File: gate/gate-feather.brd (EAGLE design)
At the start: 64.8 x 91.4 mm, 32 parts, among them J1 1X21X02-BIG, U1 SN75468

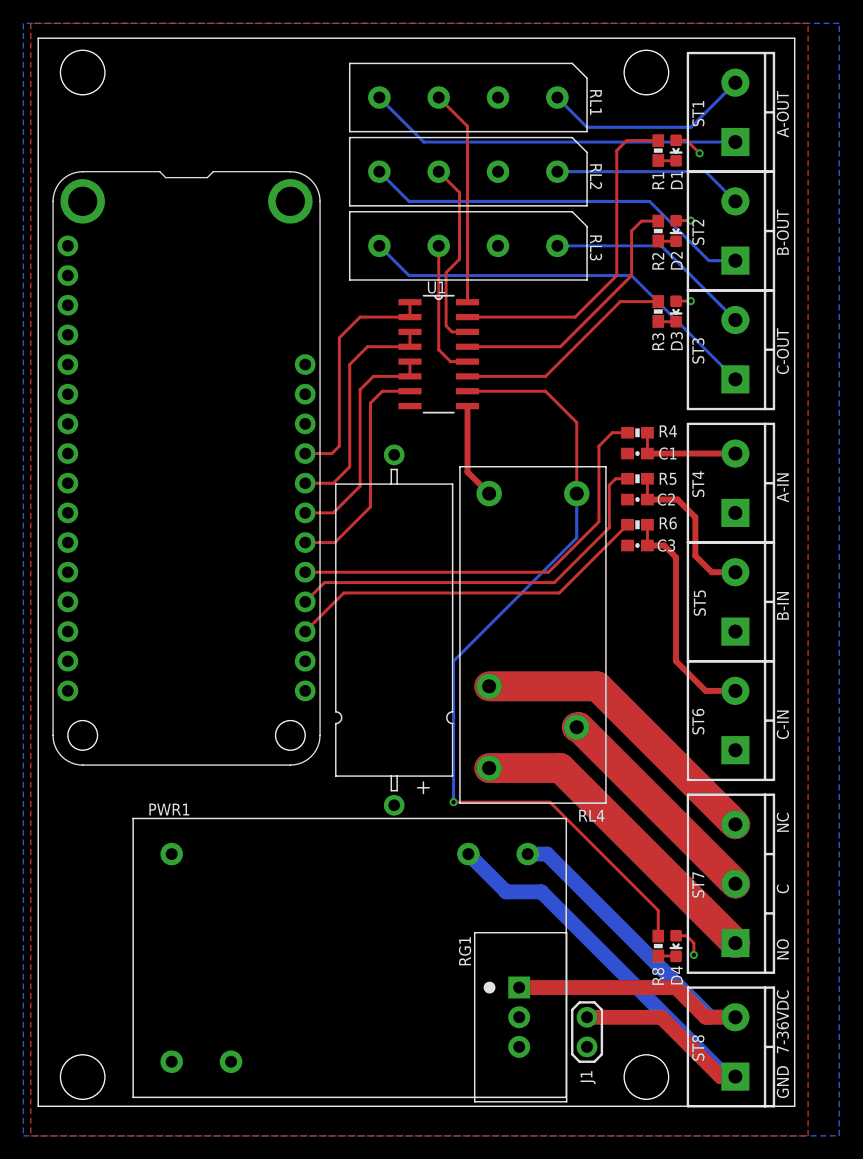
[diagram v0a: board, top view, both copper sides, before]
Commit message: New argon and feather boards
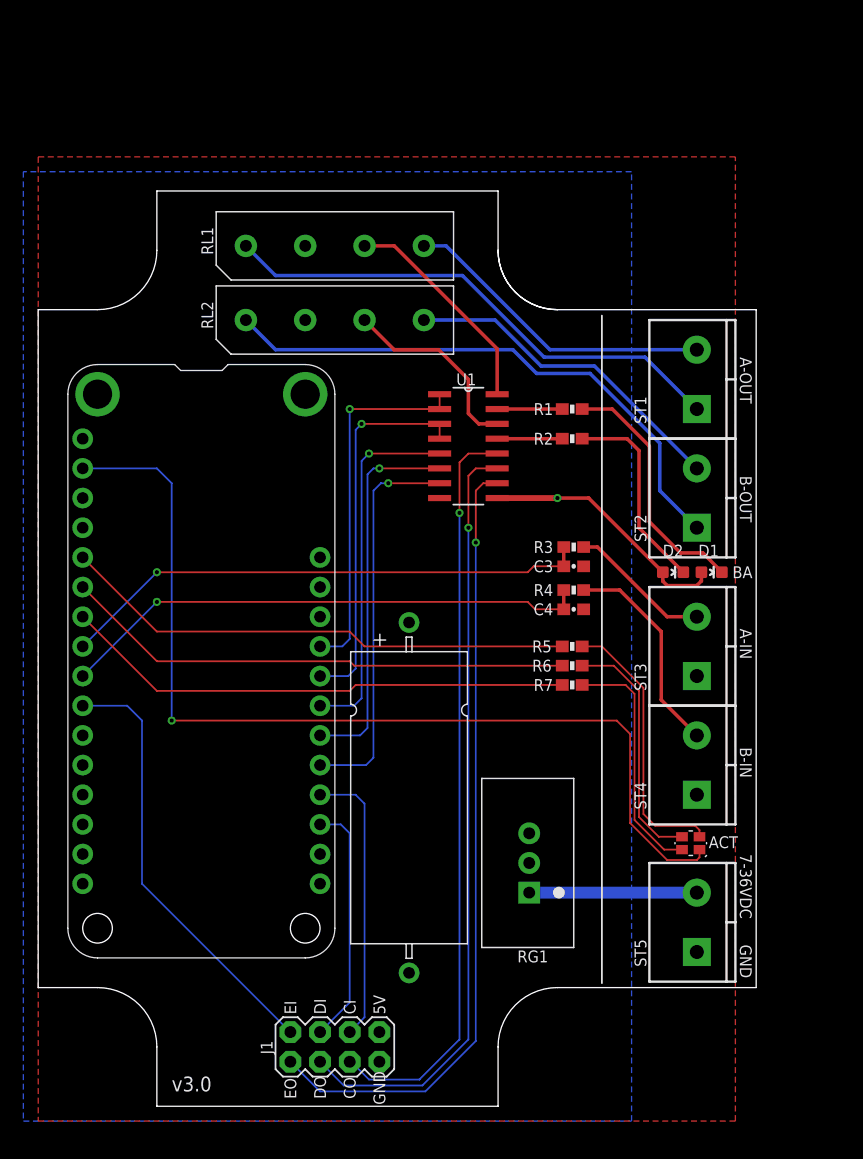
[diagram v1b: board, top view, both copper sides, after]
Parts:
- removed C2: .01u, SparkFun-Capacitors:0603-CAP
- removed D3, D4: (no value), SparkFun-LED:LED-0603
- removed MS2: FEATHERWING_NODIM, adafruit:FEATHERWING_DIM
- removed PWR1: IRM_03_PS_3W, Puffin:IRM_03_PS_3W
- removed R8: 2.2K, SparkFun-Resistors:0603-RES
- removed RL3: HE3600_RELAY, Puffin:HE3600_RELAY
- removed RL4: G2RL_SPDT, Puffin:G2RL_SPDT
- removed ST6, ST8: (no value), Puffin:SCREWTERM_0.2X2
- removed ST7: (no value), Puffin:SCREWTERM_0.2X3
- added LED1: LED-RGB-CREE-SMD, SomUSB1:LED-RGB-CREE-SMD
- added MS1: FEATHERWING_NODIM, adafruit:FEATHERWING_DIM
- added R7: 1K, SparkFun-Resistors:0603-RES
- C1: value .01u -> (none); device SparkFun-Capacitors:0603-CAP -> Puffin:CAP-AXIAL-10X25
- C4: value (none) -> .01u; device Puffin:CAP-AXIAL-10X25 -> SparkFun-Capacitors:0603-CAP
- J1: value 1X21X02-BIG -> (none); device Puffin:1X02-BIG -> SparkFun-Connectors:2X4
- R3: value 2.2K -> 1K
- moved D1 36.2 mm to (57.7, 45.7), turned to 270 degrees
- moved C1 35.4 mm to (31.8, 26.4), turned to 90 degrees
- moved RL1 29.5 mm to (17.8, 73.7), turned to 90 degrees
- moved RL2 29.5 mm to (17.8, 67.3), turned to 90 degrees
- moved D2 29.2 mm to (54.4, 45.7), turned to 270 degrees
- moved ST5 27.6 mm to (56.4, 13.2)
- moved ST3 25.6 mm to (56.4, 36.8)
- moved ST4 24.4 mm to (56.4, 26.7)
- moved R1 23.3 mm to (45.7, 59.7), turned to 180 degrees
- moved ST1 23.1 mm to (56.4, 59.7)
- moved ST2 23.1 mm to (56.4, 49.5)
- moved J1 21.6 mm to (25.4, 5.08), turned to 180 degrees
- moved R3 21.4 mm to (45.8, 47.9), turned to 0 degrees
- moved R2 19.2 mm to (45.7, 57.1), turned to 180 degrees
- moved C4 15.5 mm to (45.8, 42.5), turned to 0 degrees
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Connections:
- removed net 3V: MS2.2
- removed net IN: PWR1.ACL, RG1.1, ST8.2
- removed net N$14: RL3.4, ST3.1
- removed net RC: RL4.C, ST7.2
- removed net RNC: RL4.NC, ST7.3
- removed net RNO: RL4.NO, ST7.1
- new net 3V3: LED1.1, MS1.2
- new net N$21: MS1.22, U1.6
- new net N$24: J1.5, MS1.19
- new net N$25: J1.7, MS1.10
- new net N$8: MS1.23, U1.5
- new net VIN: RG1.1, ST5.2
- net 5V: now also C1.+, J1.1, MS1.26; no longer C4.+, D3.A, D4.A, MS2.26, PWR1.V+, RL3.2, RL4.5
- net GND: now also C1.-, C4.2, J1.2, MS1.4, ST3.1; no longer C1.2, C2.2, C4.-, J1.1, MS2.4, PWR1.V-, ST6.1
- net L5: now also J1.4; no longer RL3.3
- net L6: now also J1.6; no longer R3.2
- net L7: now also J1.8; no longer R8.2, RL4.1
- net N$10: now also LED1.4, R5.2; no longer RL3.1, ST3.2
- net N$11: now also LED1.3, R6.2; no longer MS2.22, U1.7
- net N$12: now also LED1.2, R7.2; no longer C3.1, R6.1, ST6.2
- net N$13: now also ST1.1; no longer ST1.2
- net N$15: now also MS1.6, R6.1; no longer D3.C, R3.1
- net N$16: now also MS1.5, R5.1; no longer MS2.21, R4.2
- net N$17: now also R4.2, ST4.2; no longer MS2.20, R5.2
- net N$18: now also R3.2, ST3.2; no longer MS2.19, R6.2
- net N$19: now also MS1.7, R7.1; no longer MS2.23, U1.5, U1.6
- net N$2: now also ST1.2; no longer ST1.1
- net N$20: now also J1.3, MS1.20; no longer J1.2, PWR1.ACN, ST8.1
- net N$23: now also MS1.21, U1.7; no longer D4.C, R8.1
- net N$26: now also MS1.25; no longer MS2.25
- net N$27: now also MS1.24; no longer MS2.24
- net N$31: now also C3.1, MS1.8, R3.1; no longer C1.1, R4.1, ST4.2
- net N$4: now also ST2.2; no longer ST2.1
- net N$7: now also C4.1, MS1.9, R4.1; no longer C2.1, R5.1, ST5.2
- net N$9: now also ST2.1; no longer ST2.2
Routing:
- net 3V3: track 0.00 -> 83.8 mm, vias 0 -> 1
- net RNO: track 54.6 -> 0.00 mm
- net L5: track 11.8 -> 64.4 mm, vias 0 -> 1
- net RNC: track 52.0 -> 0.00 mm
- net L6: track 19.0 -> 66.2 mm, vias 0 -> 1
- net IN: track 43.1 -> 0.00 mm
- net N$15: track 1.54 -> 43.8 mm
- net RC: track 38.3 -> 0.00 mm
- net N$25: track 0.00 -> 37.5 mm
- net N$31: track 9.31 -> 45.7 mm, vias 0 -> 1
- net N$14: track 35.2 -> 0.00 mm
- net N$21: track 0.00 -> 32.4 mm, vias 0 -> 1
- net N$23: track 1.54 -> 33.6 mm, vias 0 -> 1
- net N$9: track 16.3 -> 48.4 mm
- net N$7: track 13.8 -> 45.7 mm, vias 0 -> 1
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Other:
- board size 64.8 x 91.4 mm -> 61.5 x 78.4 mm
- board text added: "5V"
- board text added: "ACT"
- board text added: "BA"
- board text added: "CI"
- board text added: "CO"
- board text added: "DI"
- board text added: "DO"
- board text added: "EI"
- board text added: "EO"
- board text added: "v3.0"
- board text removed: "C"
- board text removed: "C-IN"
- board text removed: "C-OUT"
- board text removed: "NC"
- board text removed: "NO"
